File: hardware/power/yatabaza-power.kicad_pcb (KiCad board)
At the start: 2 copper layers, 46.4 x 60.3 mm, 34 parts, among them CON1 POWER, P1 DCDC_DUAL, P10 12V, P2 BATT, P3 PWRSW, P4 POWER, P5 HV, P6 SUPPORT, P7 SCREW, P8 SCREW, P9 12V, Q1 BC338, Q2 BC328, Q3 BC338, Q4 BC328

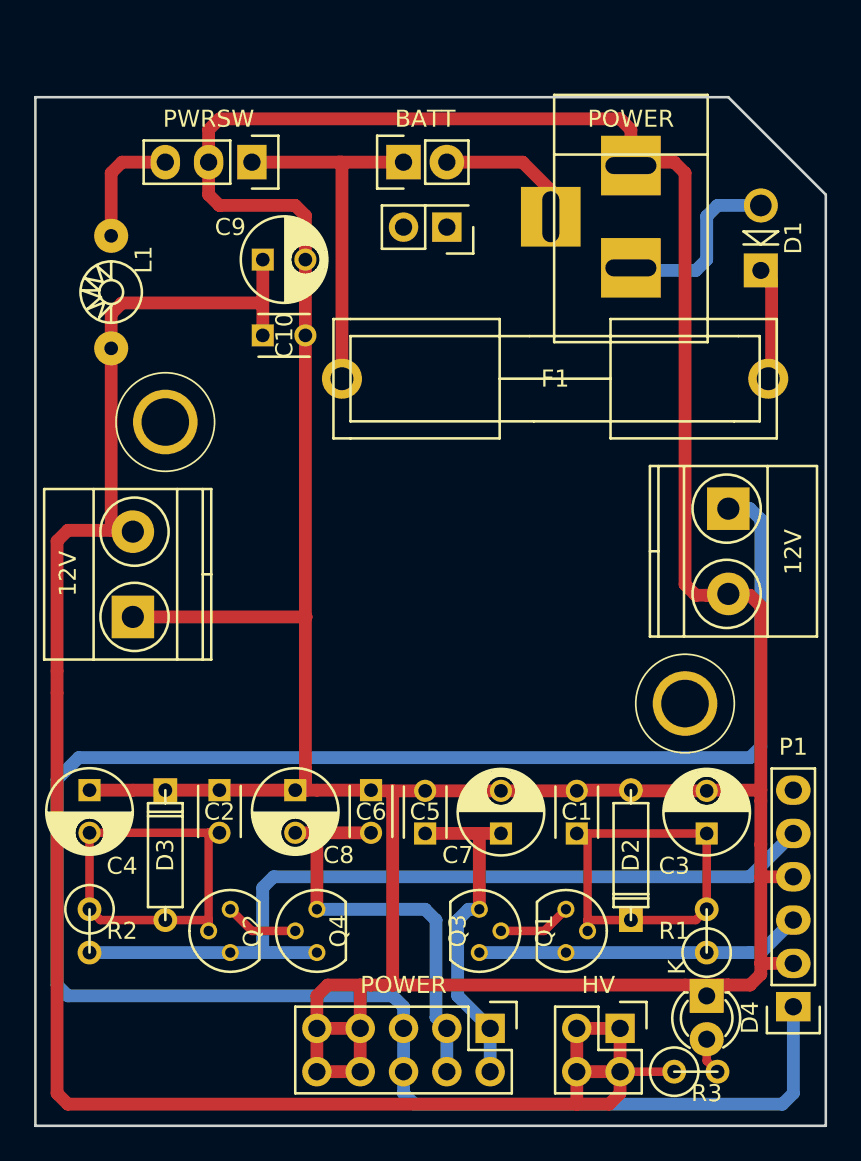
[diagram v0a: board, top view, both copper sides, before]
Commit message: ~ Ported hardware to Kicad6
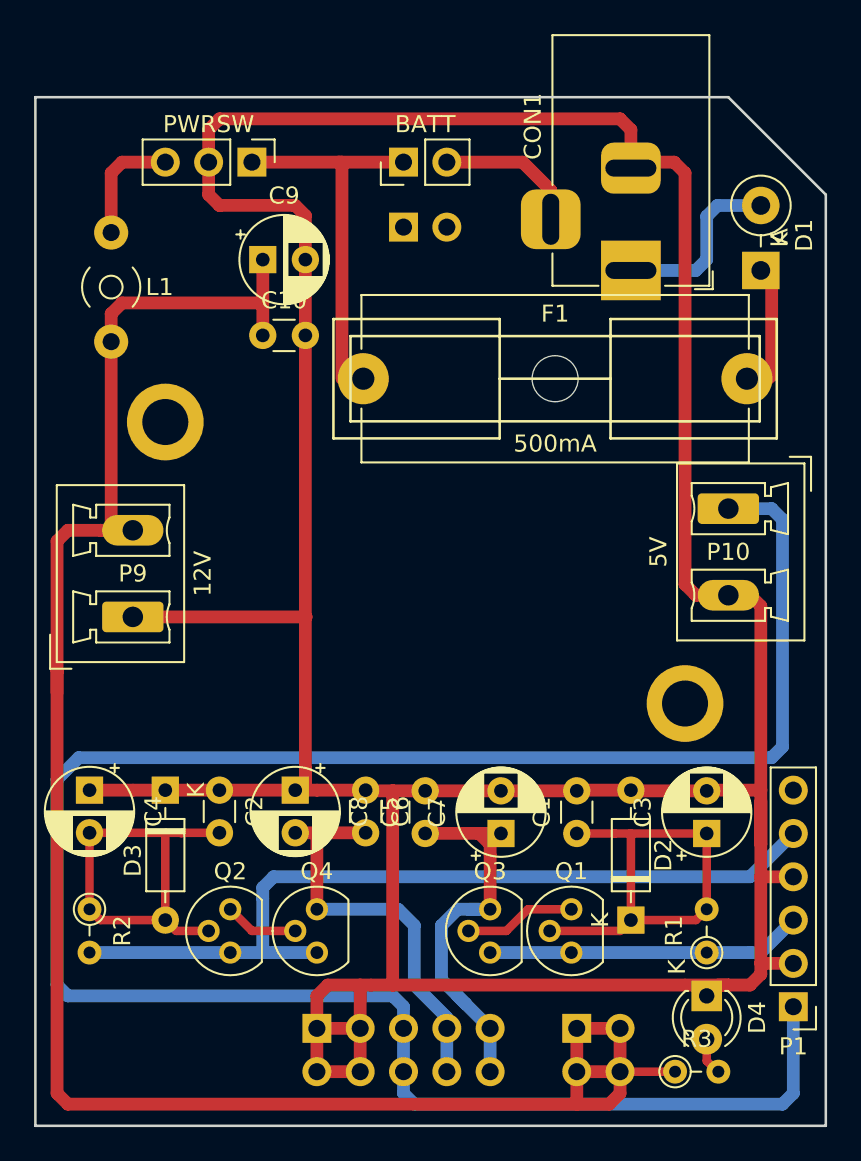
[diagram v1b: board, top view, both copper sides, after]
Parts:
- C1, C10, C2, C5, C6: footprint Capacitors_ThroughHole:C_Disc_D3_P2.5 -> Capacitor_THT:C_Disc_D3.0mm_W1.6mm_P2.50mm
- C3, C4, C7, C8, C9: footprint Capacitors_ThroughHole:C_Radial_D5_L6_P2.5 -> Capacitor_THT:CP_Radial_D5.0mm_P2.50mm
- CON1: footprint Connect:BARREL_JACK -> Connector_BarrelJack:BarrelJack_Horizontal
- D1: footprint Diodes_ThroughHole:Diode_DO-41_SOD81_Vertical_AnodeUp -> Diode_THT:D_DO-41_SOD81_P3.81mm_Vertical_KathodeUp
- D2, D3: footprint Discret:D3 -> Diode_THT:D_DO-35_SOD27_P7.62mm_Horizontal
- D4: footprint LEDs:LED-3MM -> LED_THT:LED_D3.0mm
- F1: footprint Fuse_Holders_and_Fuses:Fuseholder5x20_horiz_open_inline_Type-I -> Fuse:Fuseholder_Cylinder-5x20mm_Schurter_0031_8201_Horizontal_Open
- L1: footprint Choke_Toroid_ThroughHole:Choke_Toroid_horizontal_Diameter3-5mm_Amidon-T12 -> Inductor_THT:L_Toroid_Horizontal_D3.2mm_P6.40mm_Diameter3-5mm_Amidon-T12
- P1: footprint Pin_Headers:Pin_Header_Straight_1x06 -> Connector_PinHeader_2.54mm:PinHeader_1x06_P2.54mm_Vertical
- P10: value 12V -> 5V; footprint Terminal_Blocks:TerminalBlock_Pheonix_MKDS1.5-2pol -> Connector_Phoenix_MC_HighVoltage:PhoenixContact_MCV_1,5_2-G-5.08_1x02_P5.08mm_Vertical
- P2: footprint Pin_Headers:Pin_Header_Straight_1x02 -> Connector_PinHeader_2.54mm:PinHeader_1x02_P2.54mm_Vertical
- P3: footprint Pin_Headers:Pin_Header_Straight_1x03 -> Connector_PinHeader_2.54mm:PinHeader_1x03_P2.54mm_Vertical
- P4: footprint Pin_Headers:Pin_Header_Straight_2x05 -> Connector_PinHeader_2.54mm:PinHeader_2x05_P2.54mm_Vertical; moved to B.Cu
- P5: footprint Pin_Headers:Pin_Header_Straight_2x02 -> Connector_PinHeader_2.54mm:PinHeader_2x02_P2.54mm_Vertical; moved to B.Cu
- P6: footprint Pin_Headers:Pin_Header_Straight_2x01 -> Connector_PinHeader_2.54mm:PinHeader_1x02_P2.54mm_Vertical; moved to B.Cu
- P7, P8: footprint digikey-footprints:Test-Point-Pin_Drill2.79mm -> MountingHole:MountingHole_2.7mm_M2.5_ISO14580_Pad
- P9: footprint Terminal_Blocks:TerminalBlock_Pheonix_MKDS1.5-2pol -> Connector_Phoenix_MC_HighVoltage:PhoenixContact_MCV_1,5_2-G-5.08_1x02_P5.08mm_Vertical
- Q1, Q2, Q3, Q4: footprint TO_SOT_Packages_THT:TO-92_Molded_Narrow -> Package_TO_SOT_THT:TO-92
- R1, R2, R3: footprint Discret:R1 -> Resistor_THT:R_Axial_DIN0204_L3.6mm_D1.6mm_P2.54mm_Vertical
- moved F1 11.2 mm to (56.3, 28.6)
- moved P4 10.2 mm to (31.1, 66.7)
- moved CON1 6.35 mm to (49.5, 22.2)
- moved D2 3.81 mm to (49.5, 60.3), turned to 90 degrees
- moved D3 3.81 mm to (22.2, 52.7), turned to -90 degrees
- moved L1 3.49 mm to (19.1, 20.0)
- moved Q3 2.62 mm to (41.3, 62.2), turned to 90 degrees
- moved Q1 2.56 mm to (46.0, 62.2), turned to 90 degrees
- moved P5 2.54 mm to (46.4, 66.7)
- moved P6 2.54 mm to (36.2, 19.7), turned to -90 degrees
- moved R2 1.27 mm to (17.8, 59.7)
- moved R1 1.27 mm to (54.0, 62.2)
- moved R3 1.22 mm to (52.1, 69.2)
- moved C6 0.32 mm to (34.0, 52.7)
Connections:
- P1 pad 6: Net-(P1-Pad6) -> unconnected-(P1-Pad6)
- P4 pad 1: +9VA -> GND
- P4 pad 10: GND -> +9VA
- P4 pad 2: +9VA -> GND
- P4 pad 3: -9VA -> GND
- P4 pad 4: -9VA -> GND
- P4 pad 7: GND -> -9VA
- P4 pad 8: GND -> -9VA
- P4 pad 9: GND -> +9VA
- P6 pad 1: Net-(P6-Pad1) -> unconnected-(P6-Pad1)
- P6 pad 2: Net-(P6-Pad2) -> unconnected-(P6-Pad2)
- P7 pad 1: Net-(P7-Pad1) -> unconnected-(P7-Pad1)
- P8 pad 1: Net-(P8-Pad1) -> unconnected-(P8-Pad1)
- Q1 pad 1: Net-(Q1-Pad1) -> Net-(P1-Pad3)
- Q1 pad 3: Net-(P1-Pad3) -> Net-(Q3-Pad2)
- Q3 pad 1: +9VA -> Net-(P1-Pad3)
- Q3 pad 2: Net-(Q1-Pad1) -> Net-(Q3-Pad2)
- Q3 pad 3: Net-(P1-Pad3) -> +9VA
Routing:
- net Net-(Q3-Pad2): track 0.00 -> 6.56 mm
- net Net-(Q1-Pad1): track 4.34 -> 0.00 mm
- net +9VA: track 20.1 -> 24.4 mm
- net GND: track 234.7 -> 237.2 mm
- net +5V: track 124.0 -> 126.6 mm
- net Net-(C3-Pad1): track 26.9 -> 28.8 mm
- net +12V: track 114.1 -> 115.4 mm
- net -9VA: track 25.4 -> 24.5 mm
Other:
- net class Default removed
- rule pad_to_mask_clearance: 0.2 -> 0
